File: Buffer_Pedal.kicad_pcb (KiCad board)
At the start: 2 copper layers, 20.9 x 21.2 mm, 17 parts, among them Q1 J113, Q2 J113

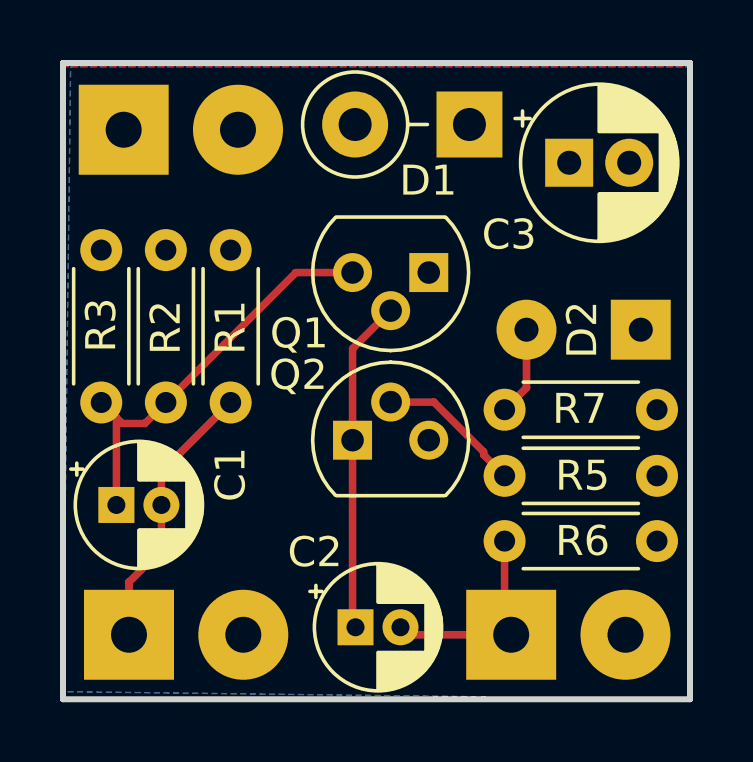
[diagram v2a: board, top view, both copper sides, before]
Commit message: larger D2 footprint
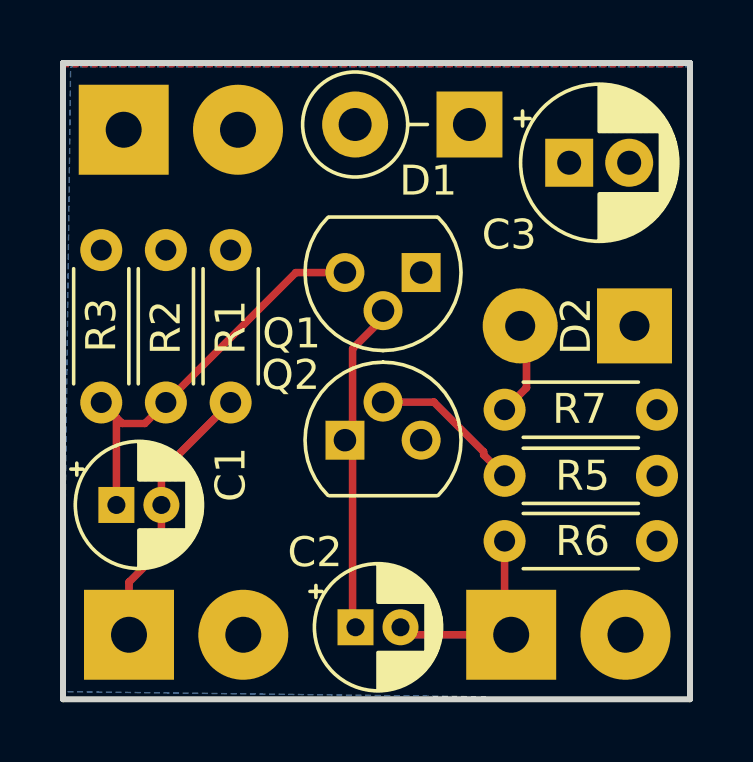
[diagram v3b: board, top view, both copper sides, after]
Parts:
- D2: footprint Connector_Wire:SolderWirePad_1x02_P3.81mm_Drill0.8mm -> Connector_Wire:SolderWirePad_1x02_P3.81mm_Drill1mm
- moved Q2 0.25 mm to (62.7, 108.2)
- moved Q1 0.25 mm to (65.3, 102.6)
- moved D2 0.25 mm to (72.4, 104.4)
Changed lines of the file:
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@@
   (page A4)
   (layers
-    (0 F.Cu signal)
-    (31 B.Cu signal)
+    (0 F.Cu signal hide)
+    (31 B.Cu signal hide)
     (32 B.Adhes user)
     (33 F.Adhes user)
@@
     (add_net "Net-(Q2-Pad2)")
     (add_net PWR)
+  )
+  (module Connector_Wire:SolderWirePad_1x02_P3.81mm_Drill1mm (layer F.Cu)
+    (at 72.39 104.394 180)
+    (descr "Wire solder connection")
+    (tags connector)
+    (attr virtual)
+    (fp_text reference D2 (at 1.95 0 90) (layer F.SilkS)
+      (effects (font (size 1 1) (thickness 0.15)))
+    )
+    (fp_text value LED (at 1.905 3.81 180) (layer F.Fab)
+      (effects (font (size 1 1) (thickness 0.15)))
+    )
+    (fp_line (start 5.56 1.75) (end -1.74 1.75) (layer F.CrtYd) (width 0.05))
+    (fp_line (start 5.56 1.75) (end 5.56 -1.75) (layer F.CrtYd) (width 0.05))
+    (fp_line (start -1.74 -1.75) (end -1.74 1.75) (layer F.CrtYd) (width 0.05))
+    (fp_line (start -1.74 -1.75) (end 5.56 -1.75) (layer F.CrtYd) (width 0.05))
+    (fp_text user %R (at 1.905 0 -90) (layer F.Fab)
+      (effects (font (size 1 1) (thickness 0.15)))
+    )
+    (pad 2 thru_hole circle (at 3.81 0 180) (size 2.49936 2.49936) (drill 1.00076) (layers *.Cu *.Mask)
+      (net 7 "Net-(D2-Pad2)"))
+    (pad 1 thru_hole rect (at 0 0 180) (size 2.49936 2.49936) (drill 1.00076) (layers *.Cu *.Mask)
+      (net 5 GND))
   )
   (module tst:Bluet (layer B.Cu)
@@
     )
   )
-  (module Connector_Wire:SolderWirePad_1x02_P3.81mm_Drill0.8mm (layer F.Cu)
-    (at 72.6 104.521 180)
-    (descr "Wire solder connection")
-    (tags connector)
-    (attr virtual)
-    (fp_text reference D2 (at 1.95 0 90) (layer F.SilkS)
-      (effects (font (size 1 1) (thickness 0.15)))
-    )
-    (fp_text value LED (at 1.905 3.81 180) (layer F.Fab)
-      (effects (font (size 1 1) (thickness 0.15)))
-    )
-    (fp_line (start 5.31 1.5) (end -1.49 1.5) (layer F.CrtYd) (width 0.05))
-    (fp_line (start 5.31 1.5) (end 5.31 -1.5) (layer F.CrtYd) (width 0.05))
-    (fp_line (start -1.49 -1.5) (end -1.49 1.5) (layer F.CrtYd) (width 0.05))
-    (fp_line (start -1.49 -1.5) (end 5.31 -1.5) (layer F.CrtYd) (width 0.05))
-    (fp_text user %R (at 1.905 0 -90) (layer F.Fab)
-      (effects (font (size 1 1) (thickness 0.15)))
-    )
-    (pad 2 thru_hole circle (at 3.81 0 180) (size 1.99898 1.99898) (drill 0.8001) (layers *.Cu *.Mask)
-      (net 7 "Net-(D2-Pad2)"))
-    (pad 1 thru_hole rect (at 0 0 180) (size 1.99898 1.99898) (drill 0.8001) (layers *.Cu *.Mask)
-      (net 5 GND))
-  )
   (module Resistor_THT:R_Axial_DIN0204_L3.6mm_D1.6mm_P5.08mm_Horizontal locked (layer F.Cu)
     (at 58.928 101.867 270)
@@
   )
   (module Package_TO_SOT_THT:TO-92 (layer F.Cu)
-    (at 62.992 108.204)
+    (at 62.738 108.204)
     (descr "TO-92 leads molded, narrow, drill 0.75mm (see NXP sot054_po.pdf)")
     (tags "to-92 sc-43 sc-43a sot54 PA33 transistor")
@@
   )
   (module Package_TO_SOT_THT:TO-92 (layer F.Cu)
-    (at 65.532 102.616 180)
+    (at 65.278 102.616 180)
     (descr "TO-92 leads molded, narrow, drill 0.75mm (see NXP sot054_po.pdf)")
     (tags "to-92 sc-43 sc-43a sot54 PA33 transistor")
